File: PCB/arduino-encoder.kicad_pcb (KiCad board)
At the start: 2 copper layers, 69.9 x 69.9 mm, 0 parts

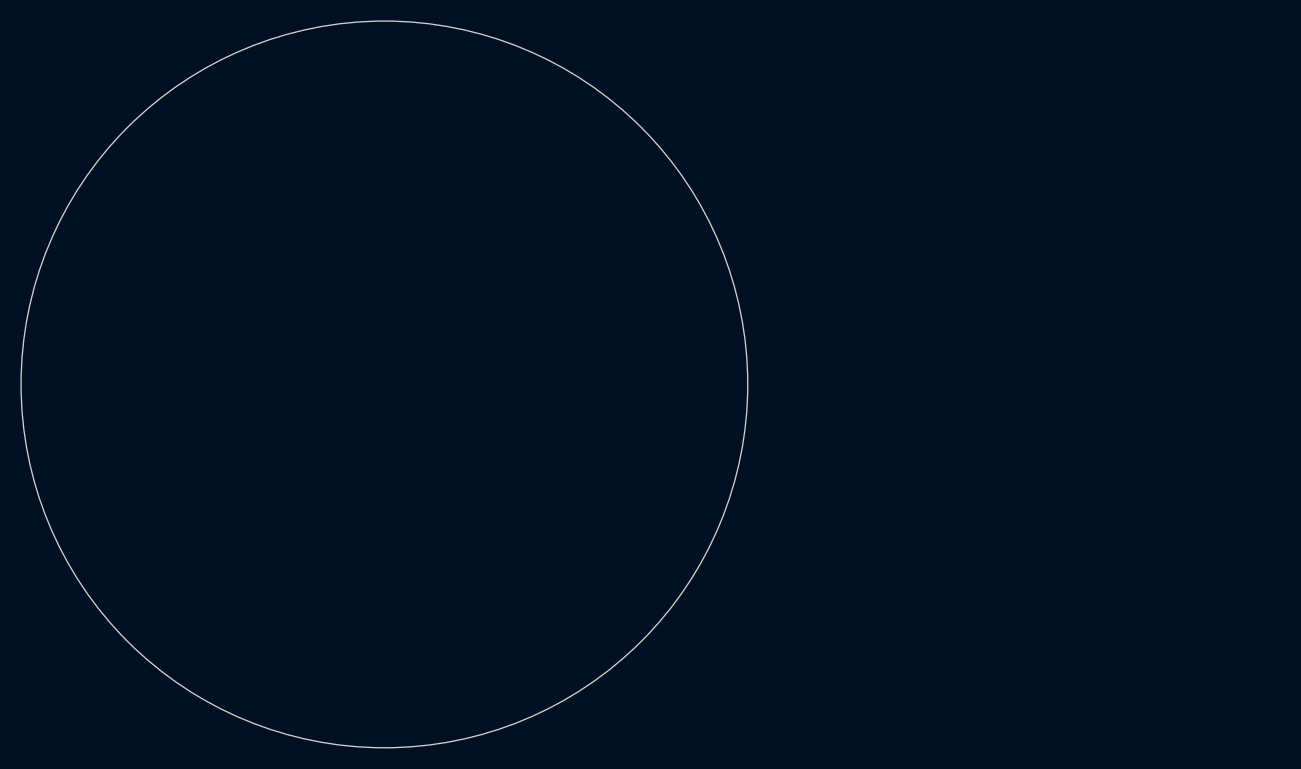
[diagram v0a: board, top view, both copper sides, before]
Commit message: add ws2812 circuit,
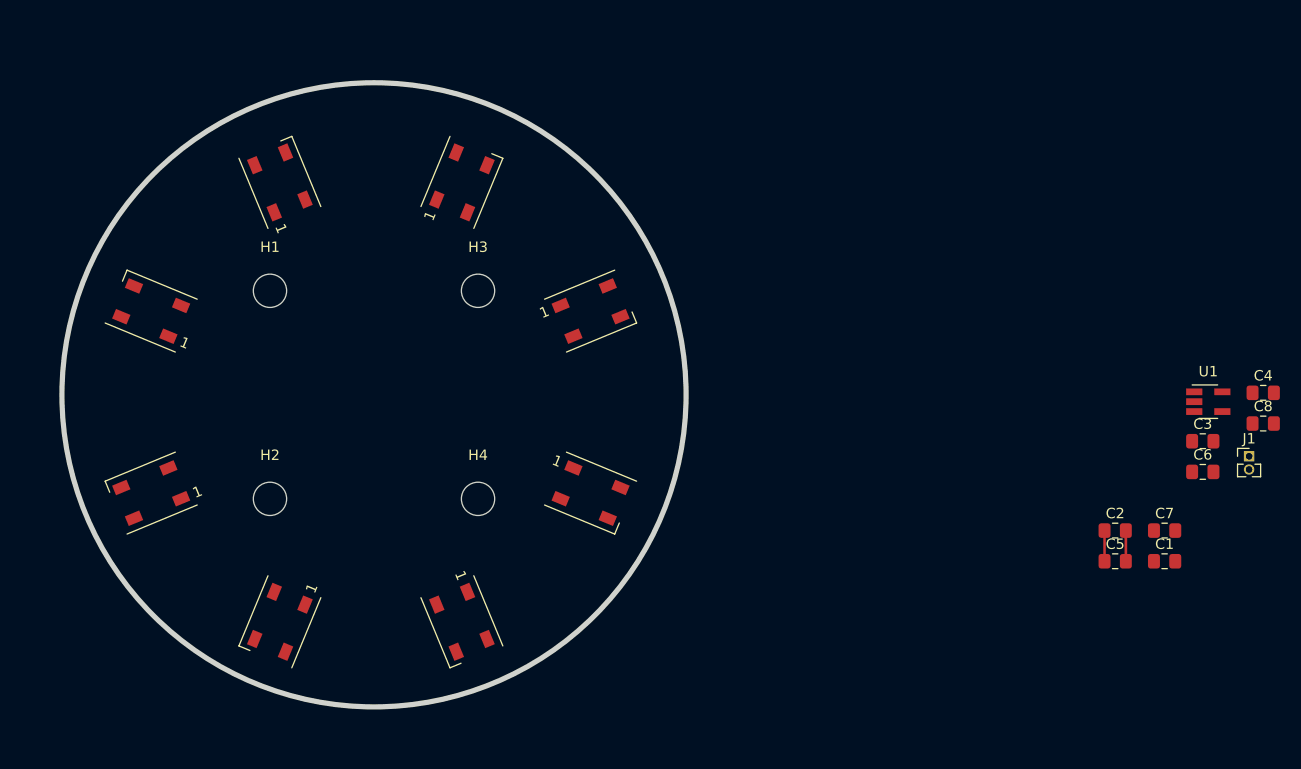
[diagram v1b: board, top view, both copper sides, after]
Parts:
- added C1: C106,0805, Capacitor_SMD:C_0805_2012Metric_Pad1.15x1.40mm_HandSolder, F.Cu at (146.0, 76.0)
- added C2: C106,0805, Capacitor_SMD:C_0805_2012Metric_Pad1.15x1.40mm_HandSolder, F.Cu at (141.2, 73.0)
- added C3: C106,0805, Capacitor_SMD:C_0805_2012Metric_Pad1.15x1.40mm_HandSolder, F.Cu at (149.7, 64.5)
- added C4: C106,0805, Capacitor_SMD:C_0805_2012Metric_Pad1.15x1.40mm_HandSolder, F.Cu at (155.5, 59.8)
- added C5: C106,0805, Capacitor_SMD:C_0805_2012Metric_Pad1.15x1.40mm_HandSolder, F.Cu at (141.2, 76.0)
- added C6: C106,0805, Capacitor_SMD:C_0805_2012Metric_Pad1.15x1.40mm_HandSolder, F.Cu at (149.7, 67.4)
- added C7: C106,0805, Capacitor_SMD:C_0805_2012Metric_Pad1.15x1.40mm_HandSolder, F.Cu at (146.0, 73.0)
- added C8: C106,0805, Capacitor_SMD:C_0805_2012Metric_Pad1.15x1.40mm_HandSolder, F.Cu at (155.5, 62.8)
- added D1: WS2812B, LED_SMD:LED_WS2812B_PLCC4_5.0x5.0mm_P3.2mm, F.Cu at (90.8, 69.4)
- added D2: WS2812B, LED_SMD:LED_WS2812B_PLCC4_5.0x5.0mm_P3.2mm, F.Cu at (78.4, 81.8)
- added D3: WS2812B, LED_SMD:LED_WS2812B_PLCC4_5.0x5.0mm_P3.2mm, F.Cu at (61.0, 81.8)
- added D4: WS2812B, LED_SMD:LED_WS2812B_PLCC4_5.0x5.0mm_P3.2mm, F.Cu at (48.6, 69.4)
- added D5: WS2812B, LED_SMD:LED_WS2812B_PLCC4_5.0x5.0mm_P3.2mm, F.Cu at (48.6, 52.0)
- added D6: WS2812B, LED_SMD:LED_WS2812B_PLCC4_5.0x5.0mm_P3.2mm, F.Cu at (61.0, 39.6)
- added D7: WS2812B, LED_SMD:LED_WS2812B_PLCC4_5.0x5.0mm_P3.2mm, F.Cu at (78.4, 39.6)
- added D8: WS2812B, LED_SMD:LED_WS2812B_PLCC4_5.0x5.0mm_P3.2mm, F.Cu at (90.8, 52.0)
- added H1: MOUNT_M3, MountingHole:MountingHole_3.2mm_M3, F.Cu at (60.0, 50.0)
- added H2: MOUNT_M3, MountingHole:MountingHole_3.2mm_M3, F.Cu at (60.0, 70.0)
- added H3: MOUNT_M3, MountingHole:MountingHole_3.2mm_M3, F.Cu at (80.0, 50.0)
- added H4: MOUNT_M3, MountingHole:MountingHole_3.2mm_M3, F.Cu at (80.0, 70.0)
- added J1: WS2812_HEADER, Connector_PinHeader_1.27mm:PinHeader_1x02_P1.27mm_Vertical, F.Cu at (154.1, 65.9)
- added U1: 74AHCT1G125, Package_TO_SOT_SMD:SOT-23-5_HandSoldering, F.Cu at (150.2, 60.7)
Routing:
- net GND: track 0.00 -> 2.95 mm
- net +5V: track 0.00 -> 2.95 mm
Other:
- board size 69.9 x 69.9 mm -> 60 x 60 mm
